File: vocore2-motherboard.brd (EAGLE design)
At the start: 100 x 100 mm, 99 parts, among them IC1 AP63205, IC2 FE1.1S, IC3 LM3671MF-3.3, IC4 LM3671MF-3.3, IC5 LM3671MF-3.3, IC7 SN74LVC2G14DBVR, IC8 FT230XS-R, J1 RJHSE-5381, J2 TE_1775470-8, J3 AMPHENOL_1140084168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

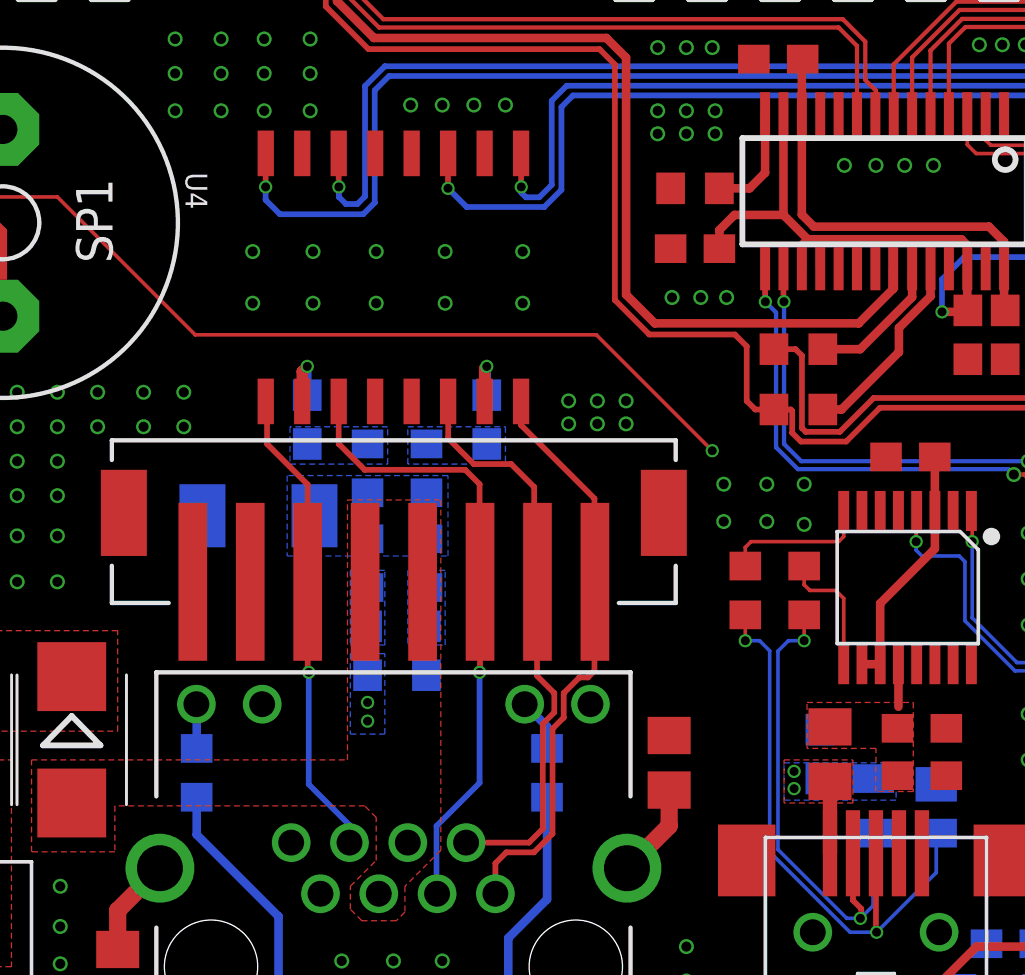
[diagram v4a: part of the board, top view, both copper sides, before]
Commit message: feat: LED für V_USB
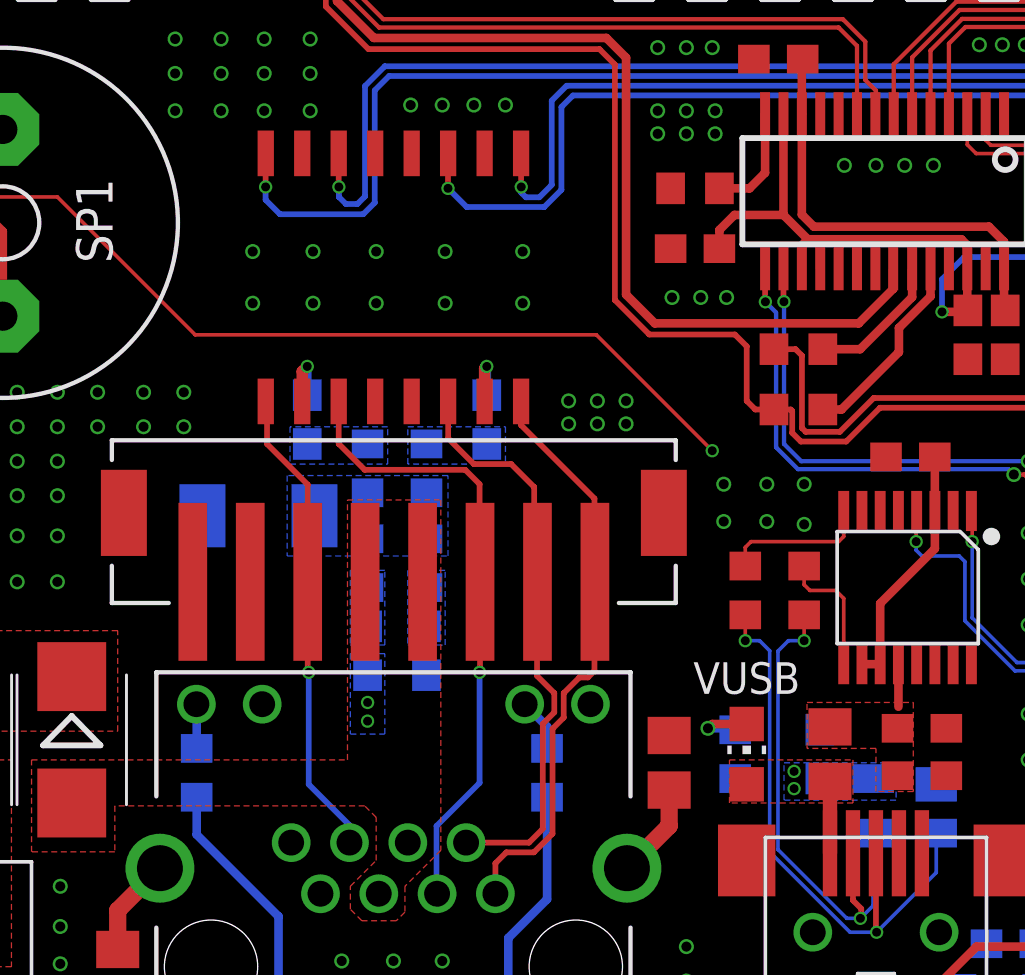
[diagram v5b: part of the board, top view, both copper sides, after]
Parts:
- added LED8: RED, led:CHIP-LED0805
- added R22: 330R, rcl:R0603
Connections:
- new net N$39: LED8.C, R22.2
- net GND: now also R22.1
- net V_USB: now also LED8.A
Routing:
- net N$39: track 0.00 -> 2.38 mm, vias 0 -> 1
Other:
- board text added: "VUSB"
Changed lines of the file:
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@@
 <wire x1="27.94644375" y1="8.74695" x2="28.653553125" y2="8.74695" width="0.127" layer="156" curve="90"/>
 <text x="43.9" y="28" size="1.1" layer="25" rot="R90" align="bottom-center">GND</text>
+<text x="-3.7" y="12.9" size="1.1" layer="25" align="bottom-center">VUSB</text>
 </plain>
 <attributes>
@@
 <attribute name="DIGIKEY" value="507-1463-1-ND" x="-16" y="27.4" size="1.778" layer="27" rot="R270" display="off"/>
 <attribute name="LCSC" value="C172799" x="-16" y="27.4" size="1.778" layer="27" rot="R270" display="off"/>
-<attribute name="NAME" x="-23.239" y="31.0576" size="0.762" layer="25" ratio="6" rot="SR270"/>
 </element>
 <element name="IC8" library="ftdi" package="SSOP16-0.635-5X4MM" value="FT230XS-R" x="1.9" y="16.6" smashed="yes" rot="R180">
@@
 <attribute name="SPICEPREFIX" value="C" x="5.5" y="4.2" size="1.778" layer="28" rot="MR0" display="off"/>
 </element>
+<element name="LED8" library="led" library_urn="urn:adsk.eagle:library:259" package="CHIP-LED0805" package3d_urn="urn:adsk.eagle:package:15818/2" value="RED" x="-3.7" y="10.8" smashed="yes">
+<attribute name="DIGIKEY" value="160-1447-1-ND" x="-9.9" y="19.7" size="1.778" layer="27" display="off"/>
+</element>
+<element name="R22" library="rcl" library_urn="urn:adsk.eagle:library:334" package="R0603" package3d_urn="urn:adsk.eagle:package:23555/3" value="330R" x="-4.1" y="10.8" smashed="yes" rot="MR90">
+<attribute name="POPULARITY" value="70" x="4.8" y="4.6" size="1.778" layer="28" rot="MR90" display="off"/>
+<attribute name="SPICEPREFIX" value="R" x="4.8" y="4.6" size="1.778" layer="28" rot="MR90" display="off"/>
+</element>
 </elements>
 <signals>
@@
 <via x="19.4" y="32.5" extent="1-16" drill="0.35"/>
 <via x="19.4" y="34.8" extent="1-16" drill="0.35"/>
+<contactref element="R22" pad="1"/>
 </signal>
 <signal name="N$1">
@@
 <via x="-2.05" y="9.6" extent="1-16" drill="0.31"/>
 <polygon width="0.1" layer="1" thermals="no">
-<vertex x="-2.4" y="10.6"/>
+<vertex x="-4.3" y="10.6"/>
 <vertex x="0" y="10.6"/>
 <vertex x="0" y="9.1"/>
-<vertex x="-2.4" y="9.1"/>
+<vertex x="-4.3" y="9.1"/>
 </polygon>
+<contactref element="LED8" pad="A"/>
 </signal>
 <signal name="VC_3V3">
@@
 <wire x1="1.3" y1="0.9" x2="1" y2="0.6" width="0.3" layer="16"/>
 </signal>
+<signal name="N$39">
+<contactref element="LED8" pad="C"/>
+<contactref element="R22" pad="2"/>
+<wire x1="-3.7" y1="11.85" x2="-4.9" y2="11.85" width="0.3" layer="1"/>
+<wire x1="-4.9" y1="11.85" x2="-5.05" y2="11.7" width="0.3" layer="1"/>
+<via x="-5.05" y="11.7" extent="1-16" drill="0.35"/>
+<wire x1="-4.15" y1="11.7" x2="-4.1" y2="11.65" width="0.3" layer="16"/>
+<wire x1="-4.15" y1="11.7" x2="-5.05" y2="11.7" width="0.3" layer="16"/>
+</signal>
 </signals>

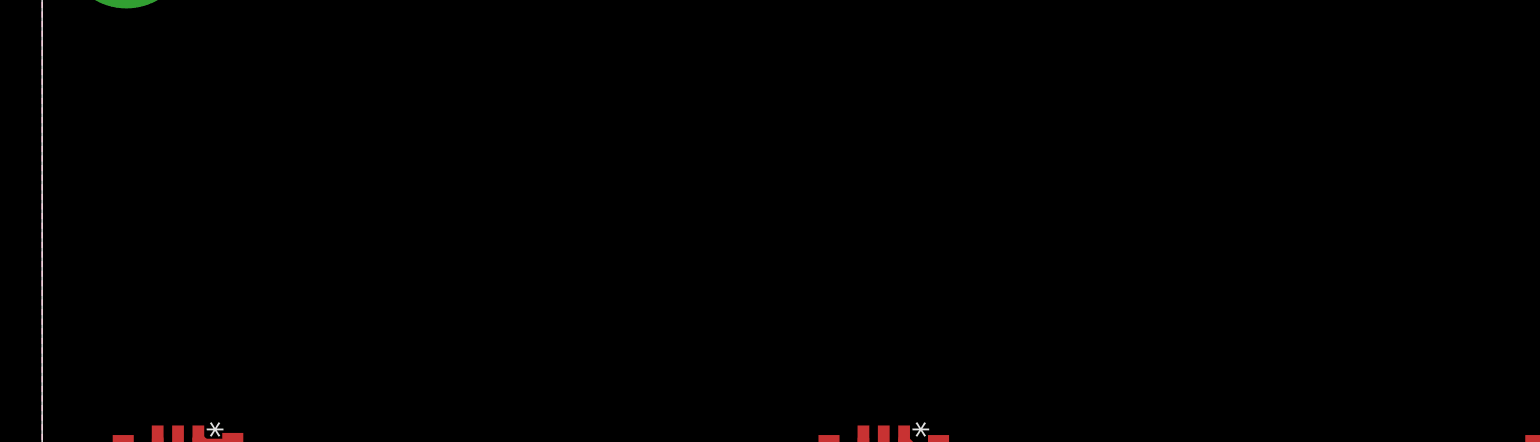
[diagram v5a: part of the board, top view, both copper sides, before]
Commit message: feat(brd): threaded inserts for PCIe half-sized card (X3 and X2 only)
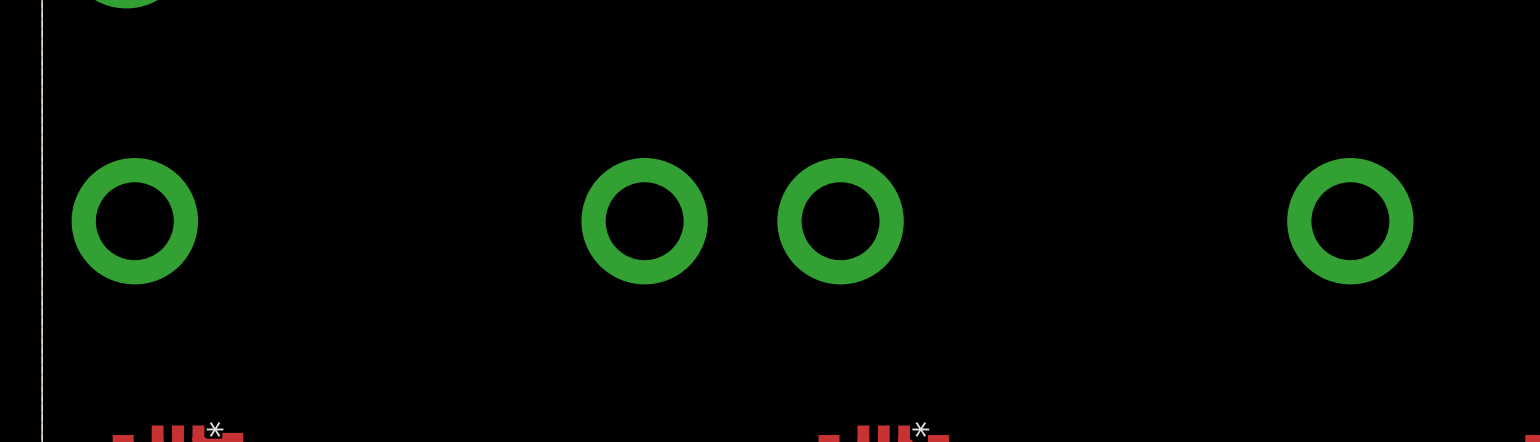
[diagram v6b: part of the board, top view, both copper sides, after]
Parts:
- X1: value TE_1775838-2 -> TE_1775838-2-FULL; device pachl-con:TE_1775838-2 -> pachl-con:TE_1775838-2-FULL
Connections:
- net GND: now also X2.P$3, X2.P$4, X3.P$3, X3.P$4
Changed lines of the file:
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@@
 <attribute name="POPULARITY" value="2" x="-29.6" y="29.3" size="1.778" layer="27" rot="R270" display="off"/>
 </element>
-<element name="X1" library="pachl-con" package="TE_1775838-2" value="TE_1775838-2" x="33.5" y="48" smashed="yes">
-<attribute name="CENTERLINE_PITCH" value=".8 mm[.031 in]" x="33.5" y="48" size="1.778" layer="27" display="off"/>
-<attribute name="COMMENT" value="1775838-2" x="33.5" y="48" size="1.778" layer="27" display="off"/>
-<attribute name="DESCRIPTION" value=" mSATA/mini PCI-E 5.6H Type I G/F " x="33.5" y="48" size="1.778" layer="27" display="off"/>
-<attribute name="DIGI-KEY_PART_NUMBER" value="A123340CT-ND" x="33.5" y="48" size="1.778" layer="27" display="off"/>
-<attribute name="DIGI-KEY_PURCHASE_URL" value="https://www.digikey.com/product-detail/en/te-connectivity-amp-connectors/1775838-2/A123340CT-ND/5451751?utm_source=snapeda&amp;utm_medium=aggregator&amp;utm_campaign=symbol" x="33.5" y="48" size="1.778" layer="27" display="off"/>
-<attribute name="EU_ROHS_COMPLIANCE" value="Compliant" x="33.5" y="48" size="1.778" layer="27" display="off"/>
-<attribute name="MF" value="TE Connectivity" x="33.5" y="48" size="1.778" layer="27" display="off"/>
-<attribute name="MP" value="1775838-2" x="33.5" y="48" size="1.778" layer="27" display="off"/>
+<element name="X1" library="pachl-con" package="TE_1775838-2-FULL" value="TE_1775838-2-FULL" x="33.5" y="48" smashed="yes">
 <attribute name="NAME" x="18.3769" y="41.1137" size="1.27193125" layer="25"/>
-<attribute name="NUMBER_OF_POSITIONS" value="52" x="33.5" y="48" size="1.778" layer="27" display="off"/>
-<attribute name="PACKAGE" value="None" x="33.5" y="48" size="1.778" layer="27" display="off"/>
-<attribute name="PRODUCT_TYPE" value="Connector" x="33.5" y="48" size="1.778" layer="27" display="off"/>
-<attribute name="TE_PURCHASE_URL" value="https://www.te.com/usa-en/product-1775838-2.html?te_bu=Cor&amp;te_type=disp&amp;te_campaign=seda_glo_cor-seda-global-disp-prtnr-fy19-seda-model-bom-cta_sma-317_1&amp;elqCampaignId=32493" x="33.5" y="48" size="1.778" layer="27" display="off"/>
 </element>
 <element name="IC2" library="Ai_IC" package="FE1.1S_SSOP-28" value="FE1.1S" x="1.1" y="30.4" smashed="yes" rot="R180">
@@
 <signals>
 <signal name="GND">
-<contactref element="X3" pad="P$1"/>
-<contactref element="X3" pad="P$2"/>
-<contactref element="X2" pad="P$1"/>
-<contactref element="X2" pad="P$2"/>
 <polygon width="0.1" layer="1" rank="2">
 <vertex x="-50" y="100"/>
@@
 <via x="-33.9" y="1.6" extent="1-16" drill="0.31"/>
 <via x="-33.2" y="1.6" extent="1-16" drill="0.31"/>
-<contactref element="X1" pad="P$1"/>
-<contactref element="X1" pad="P$2"/>
 <contactref element="IC2" pad="1"/>
 <contactref element="C3" pad="2"/>
@@
 <via x="19.4" y="34.8" extent="1-16" drill="0.35"/>
 <contactref element="R22" pad="1"/>
+<contactref element="X3" pad="P$1"/>
+<contactref element="X3" pad="P$3"/>
+<contactref element="X3" pad="P$4"/>
+<contactref element="X3" pad="P$2"/>
+<contactref element="X2" pad="P$1"/>
+<contactref element="X2" pad="P$3"/>
+<contactref element="X2" pad="P$4"/>
+<contactref element="X2" pad="P$2"/>
+<contactref element="X1" pad="P$1"/>
+<contactref element="X1" pad="P$2"/>
 </signal>
 <signal name="N$1">

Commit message: fix: changed led resistor values
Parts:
- R10, R6: value 150R -> 100R
- R2, R4, R5: value 150R -> 470R
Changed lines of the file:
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@@
 <attribute name="DIGIKEY" value="160-1445-1-ND" x="44.3" y="39.6" size="1.778" layer="27" display="off"/>
 </element>
-<element name="R2" library="rcl" library_urn="urn:adsk.eagle:library:334" package="R0603" package3d_urn="urn:adsk.eagle:package:23555/3" value="150R" x="44.3" y="39.6" smashed="yes" rot="MR90">
+<element name="R2" library="rcl" library_urn="urn:adsk.eagle:library:334" package="R0603" package3d_urn="urn:adsk.eagle:package:23555/3" value="470R" x="44.3" y="39.6" smashed="yes" rot="MR90">
 <attribute name="POPULARITY" value="70" x="44.3" y="39.6" size="1.778" layer="28" rot="MR90" display="off"/>
 <attribute name="SPICEPREFIX" value="R" x="51.8" y="33.4" size="1.778" layer="28" rot="MR90" display="off"/>
@@
 <attribute name="DIGIKEY" value="160-1445-1-ND" x="10.8" y="39.6" size="1.778" layer="27" display="off"/>
 </element>
-<element name="R4" library="rcl" library_urn="urn:adsk.eagle:library:334" package="R0603" package3d_urn="urn:adsk.eagle:package:23555/3" value="150R" x="10.8" y="39.6" smashed="yes" rot="MR90">
+<element name="R4" library="rcl" library_urn="urn:adsk.eagle:library:334" package="R0603" package3d_urn="urn:adsk.eagle:package:23555/3" value="470R" x="10.8" y="39.6" smashed="yes" rot="MR90">
 <attribute name="POPULARITY" value="70" x="10.8" y="39.6" size="1.778" layer="28" rot="MR90" display="off"/>
 <attribute name="SPICEPREFIX" value="R" x="18.3" y="33.4" size="1.778" layer="28" rot="MR90" display="off"/>
@@
 <attribute name="DIGIKEY" value="160-1445-1-ND" x="-22.7" y="39.6" size="1.778" layer="27" display="off"/>
 </element>
-<element name="R5" library="rcl" library_urn="urn:adsk.eagle:library:334" package="R0603" package3d_urn="urn:adsk.eagle:package:23555/3" value="150R" x="-22.7" y="39.6" smashed="yes" rot="MR90">
+<element name="R5" library="rcl" library_urn="urn:adsk.eagle:library:334" package="R0603" package3d_urn="urn:adsk.eagle:package:23555/3" value="470R" x="-22.7" y="39.6" smashed="yes" rot="MR90">
 <attribute name="POPULARITY" value="70" x="-22.7" y="39.6" size="1.778" layer="28" rot="MR90" display="off"/>
 <attribute name="SPICEPREFIX" value="R" x="-15.2" y="33.4" size="1.778" layer="28" rot="MR90" display="off"/>
@@
 <attribute name="DIGIKEY" value="160-1446-1-ND" x="-20.2" y="39.6" size="1.778" layer="27" rot="R180" display="off"/>
 </element>
-<element name="R6" library="rcl" library_urn="urn:adsk.eagle:library:334" package="R0603" package3d_urn="urn:adsk.eagle:package:23555/3" value="150R" x="-1.9" y="24.9" smashed="yes" rot="R180">
+<element name="R6" library="rcl" library_urn="urn:adsk.eagle:library:334" package="R0603" package3d_urn="urn:adsk.eagle:package:23555/3" value="100R" x="-1.9" y="24.9" smashed="yes" rot="R180">
 <attribute name="POPULARITY" value="70" x="10.5" y="17.4" size="1.778" layer="27" rot="R180" display="off"/>
 <attribute name="SPICEPREFIX" value="R" x="10.5" y="17.4" size="1.778" layer="27" rot="R180" display="off"/>
@@
 <attribute name="DIGIKEY" value="160-1446-1-ND" x="13.3" y="39.6" size="1.778" layer="27" display="off"/>
 </element>
-<element name="R10" library="rcl" library_urn="urn:adsk.eagle:library:334" package="R0603" package3d_urn="urn:adsk.eagle:package:23555/3" value="150R" x="-1.9" y="22.8" smashed="yes" rot="R180">
+<element name="R10" library="rcl" library_urn="urn:adsk.eagle:library:334" package="R0603" package3d_urn="urn:adsk.eagle:package:23555/3" value="100R" x="-1.9" y="22.8" smashed="yes" rot="R180">
 <attribute name="POPULARITY" value="70" x="10.5" y="12.7" size="1.778" layer="27" rot="R180" display="off"/>
 <attribute name="SPICEPREFIX" value="R" x="10.5" y="12.7" size="1.778" layer="27" rot="R180" display="off"/>
